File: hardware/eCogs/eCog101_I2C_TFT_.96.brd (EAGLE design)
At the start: 47.5 x 28 mm, 4 parts

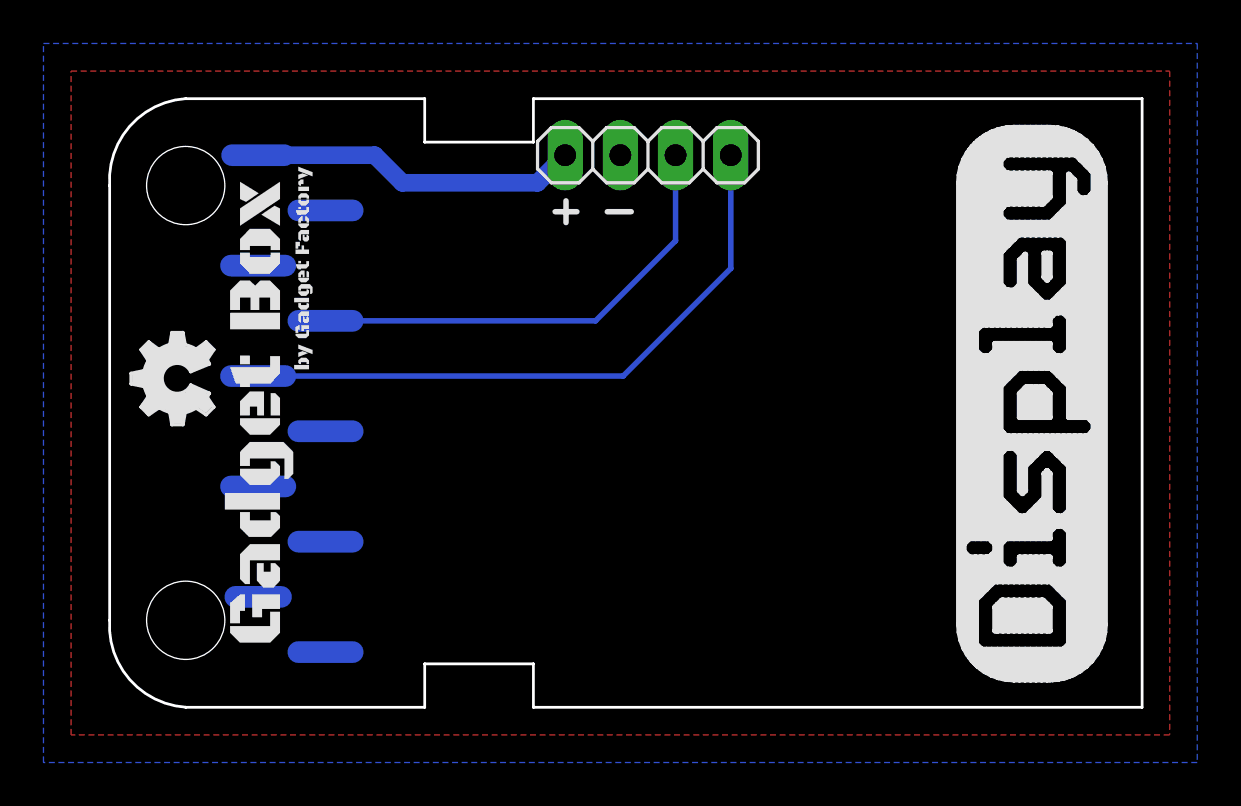
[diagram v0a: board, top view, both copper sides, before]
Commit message: Put connector for both types of power schemes.
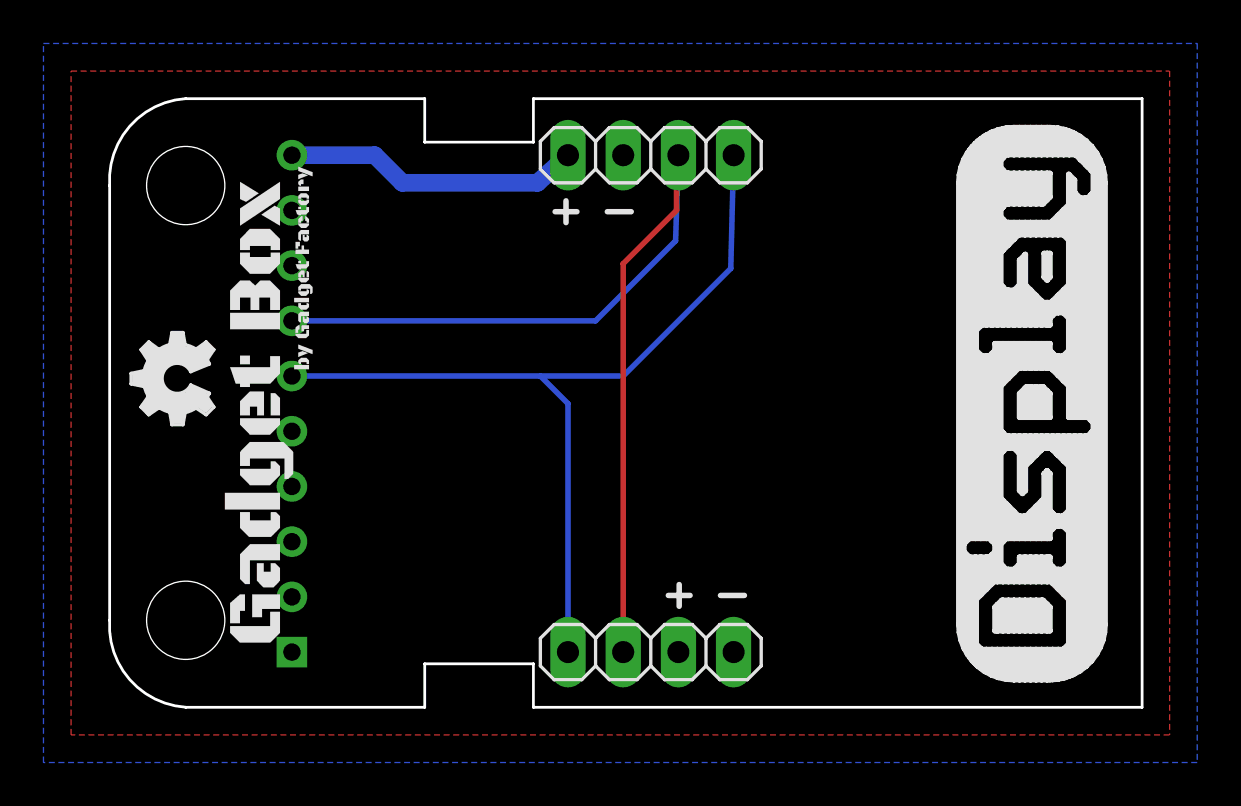
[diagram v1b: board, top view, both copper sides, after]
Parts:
- added JP2: .96 I2C OLED LCD, pinhead:1X04
- ECOG: value ECOG_BUSES_ROWSURFACEMOUNT -> ECOG_BUSES_ROWTHROUGHHOLE; device eCogs:ECOG_BUSES_SMD -> eCogs:ECOG_BUSES_TH
- moved JP1 0.13 mm to (25.4, 25.4)
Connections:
- net 3V3: now also JP2.2
- net GND: now also JP2.1
- net N$1: now also JP2.3
- net N$2: now also JP2.4
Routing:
- net N$1: track 21.6 -> 47.0 mm
- net N$2: track 29.0 -> 40.7 mm
- net 3V3: track 15.2 -> 13.7 mm
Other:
- board text added: "ecog101 v2.1"
- board text removed: "ecog101 v2.0"
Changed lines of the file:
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@@
 <setting verticaltext="up"/>
 </settings>
-<grid distance="1" unitdist="mm" unit="mm" style="lines" multiple="1" display="yes" altdistance="0.1" altunitdist="mm" altunit="mm"/>
+<grid distance="0.05" unitdist="inch" unit="inch" style="lines" multiple="1" display="yes" altdistance="0.005" altunitdist="inch" altunit="inch"/>
 <layers>
 <layer number="1" name="Top" color="4" fill="1" visible="yes" active="yes"/>
@@
 <plain>
 <text x="37.719" y="18.415" size="0.8128" layer="22" font="vector" rot="MR0">ecog101.GadgetFactory.net</text>
-<text x="40.132" y="2.159" size="1.016" layer="22" font="vector" rot="MR0">ecog101 v2.0</text>
-<text x="40.132" y="3.429" size="1.016" layer="22" font="vector" rot="MR0">OLED LCD I2C</text>
-<text x="40.132" y="4.699" size="1.016" layer="22" font="vector" rot="MR0">eCogs</text>
+<text x="43.942" y="3.429" size="1.016" layer="22" font="vector" rot="MR0">ecog101 v2.1</text>
+<text x="43.942" y="4.699" size="1.016" layer="22" font="vector" rot="MR0">OLED LCD I2C</text>
+<text x="43.942" y="5.969" size="1.016" layer="22" font="vector" rot="MR0">eCogs</text>
 <text x="18.875" y="14.732" size="1.016" layer="22" font="vector" rot="MR0">I2C-SDA</text>
 <text x="18.875" y="17.272" size="1.016" layer="22" font="vector" rot="MR0">I2C-SCL</text>
@@
 <text x="35.052" y="16.637" size="0.6096" layer="22" font="vector" rot="MR0">Gadget Factory, LLC</text>
 <text x="13.795" y="24.892" size="1.016" layer="22" font="vector" rot="MR0">3.3V</text>
-<text x="15.065" y="2.159" size="1.016" layer="22" font="vector" rot="MR0">GND</text>
+<text x="13.287" y="2.032" size="1.016" layer="22" font="vector" rot="MR0">GND</text>
 <wire x1="42.3658" y1="13.3433" x2="42.3658" y2="14.4293" width="0.254" layer="21"/>
 <wire x1="42.3658" y1="14.4293" x2="42.618" y2="14.6815" width="0.254" layer="21"/>
@@
 <wire x1="21.5" y1="22.8" x2="21.5" y2="23.3" width="0.254" layer="21"/>
 <wire x1="21.5" y1="22.8" x2="21.5" y2="22.3" width="0.254" layer="21"/>
+<wire x1="28.607" y1="5.147" x2="29.707" y2="5.147" width="0.254" layer="21"/>
+<wire x1="26.207" y1="5.147" x2="26.707" y2="5.147" width="0.254" layer="21"/>
+<wire x1="26.707" y1="5.147" x2="27.207" y2="5.147" width="0.254" layer="21"/>
+<wire x1="26.707" y1="5.147" x2="26.707" y2="5.647" width="0.254" layer="21"/>
+<wire x1="26.707" y1="5.147" x2="26.707" y2="4.647" width="0.254" layer="21"/>
 </plain>
 <attributes>
@@
 </autorouter>
 <elements>
-<element name="ECOG" library="eCogs" package="ECOG_BUSES_SMD" value="ECOG_BUSES_ROWSURFACEMOUNT" x="0" y="0" smashed="yes">
-<attribute name="DIGIKEY" value="S1013EC-10-ND" x="0" y="0" size="1.778" layer="27" display="off"/>
-</element>
-<element name="JP1" library="pinhead" package="1X04" value=".96 I2C OLED LCD" x="25.27" y="25.4" smashed="yes">
-<attribute name="VALUE" x="20.19" y="22.225" size="1.27" layer="27"/>
-<attribute name="DEALEXTREME" value="419232" x="25.27" y="25.4" size="1.778" layer="27" display="off"/>
+<element name="ECOG" library="eCogs" package="ECOG_BUSES_TH" value="ECOG_BUSES_ROWTHROUGHHOLE" x="0" y="0" smashed="yes"/>
+<element name="JP1" library="pinhead" package="1X04" value=".96 I2C OLED LCD" x="25.4" y="25.4" smashed="yes">
+<attribute name="VALUE" x="20.32" y="22.225" size="1.27" layer="27"/>
+<attribute name="DEALEXTREME" value="419232" x="25.4" y="25.4" size="1.778" layer="27" display="off"/>
 </element>
 <element name="U$1" library="GadgetFactory" package="GADGETBOX_SMALL" value="" x="7.448" y="13.649" rot="R90"/>
 <element name="U$2" library="ohw-logo" package="OSHW_FILLX150_NOTEXT" value="" x="5.3" y="13" rot="R90"/>
+<element name="JP2" library="pinhead" package="1X04" value=".96 I2C OLED LCD" x="25.4" y="2.54" smashed="yes" rot="R180">
+<attribute name="DEALEXTREME" value="419232" x="25.4" y="2.54" size="1.778" layer="27" font="vector" ratio="15" rot="R180" display="off"/>
+<attribute name="VALUE" x="30.48" y="5.715" size="1.27" layer="27" rot="R180"/>
+</element>
 </elements>
 <signals>
@@
 <contactref element="ECOG" pad="GND"/>
 <contactref element="JP1" pad="2"/>
+<contactref element="JP2" pad="1"/>
 </signal>
 <signal name="3V3">
@@
 </polygon>
 <contactref element="ECOG" pad="3V3"/>
-<wire x1="7.337490625" y1="25.4" x2="12.7" y2="25.4" width="0.8128" layer="16"/>
+<wire x1="8.89" y1="25.4" x2="12.7" y2="25.4" width="0.8128" layer="16"/>
 <wire x1="12.7" y1="25.4" x2="13.97" y2="24.13" width="0.8128" layer="16"/>
 <wire x1="13.97" y1="24.13" x2="20.19" y2="24.13" width="0.8128" layer="16"/>
-<wire x1="20.19" y1="24.13" x2="21.46" y2="25.4" width="0.8128" layer="16"/>
+<wire x1="20.19" y1="24.13" x2="21.59" y2="25.4" width="0.8128" layer="16"/>
+<contactref element="JP2" pad="2"/>
 </signal>
 <signal name="N$2">
 <contactref element="ECOG" pad="I2C-SDA"/>
 <contactref element="JP1" pad="4"/>
-<wire x1="7.337490625" y1="15.24" x2="24.13" y2="15.24" width="0.254" layer="16"/>
+<wire x1="8.89" y1="15.24" x2="20.32" y2="15.24" width="0.254" layer="16"/>
+<wire x1="20.32" y1="15.24" x2="24.13" y2="15.24" width="0.254" layer="16"/>
 <wire x1="24.13" y1="15.24" x2="29.08" y2="20.19" width="0.254" layer="16"/>
-<wire x1="29.08" y1="25.4" x2="29.08" y2="20.19" width="0.254" layer="16"/>
+<wire x1="29.21" y1="25.4" x2="29.08" y2="20.19" width="0.254" layer="16"/>
+<contactref element="JP2" pad="4"/>
+<wire x1="21.59" y1="2.54" x2="21.59" y2="13.97" width="0.254" layer="16"/>
+<wire x1="21.59" y1="13.97" x2="20.32" y2="15.24" width="0.254" layer="16"/>
 </signal>
 <signal name="N$1">
 <contactref element="JP1" pad="3"/>
 <contactref element="ECOG" pad="I2C-SCL"/>
-<wire x1="10.436290625" y1="17.78" x2="22.86" y2="17.78" width="0.254" layer="16"/>
+<wire x1="8.89" y1="17.78" x2="22.86" y2="17.78" width="0.254" layer="16"/>
 <wire x1="22.86" y1="17.78" x2="26.54" y2="21.46" width="0.254" layer="16"/>
-<wire x1="26.54" y1="25.4" x2="26.54" y2="21.46" width="0.254" layer="16"/>
+<wire x1="26.67" y1="25.4" x2="26.54" y2="21.46" width="0.254" layer="16"/>
+<contactref element="JP2" pad="3"/>
+<wire x1="24.13" y1="2.54" x2="24.13" y2="20.406478125" width="0.254" layer="1"/>
+<wire x1="24.13" y1="20.406478125" x2="26.586284375" y2="22.8627625" width="0.254" layer="1"/>
+<wire x1="26.586284375" y1="22.8627625" x2="26.586284375" y2="25.316284375" width="0.254" layer="1"/>
+<wire x1="26.586284375" y1="25.316284375" x2="26.67" y2="25.4" width="0.254" layer="1"/>
 </signal>
 </signals>
